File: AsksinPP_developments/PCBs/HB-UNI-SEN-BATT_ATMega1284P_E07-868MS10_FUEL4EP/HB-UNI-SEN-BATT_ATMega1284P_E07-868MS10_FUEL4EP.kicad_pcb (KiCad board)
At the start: 2 copper layers, 75 x 75 mm, 56 parts, among them J1 Conn_01x02, J10 charge, J11 ePaper connector, J12 FTDI Debuger, J2 Conn_01x02, J3 Conn_01x02, J4 Conn_01x02, J5 ISP Programmer, J6 Conn_01x04, J7 Conn_01x04, J8 Conn_01x04, J9 Conn_01x04, Q1 IRLU024N, SW1 Config button, SW2 Reset button, U1 ATmega1284P-AU, U2 TPS61221DCK, Y1 8MHz

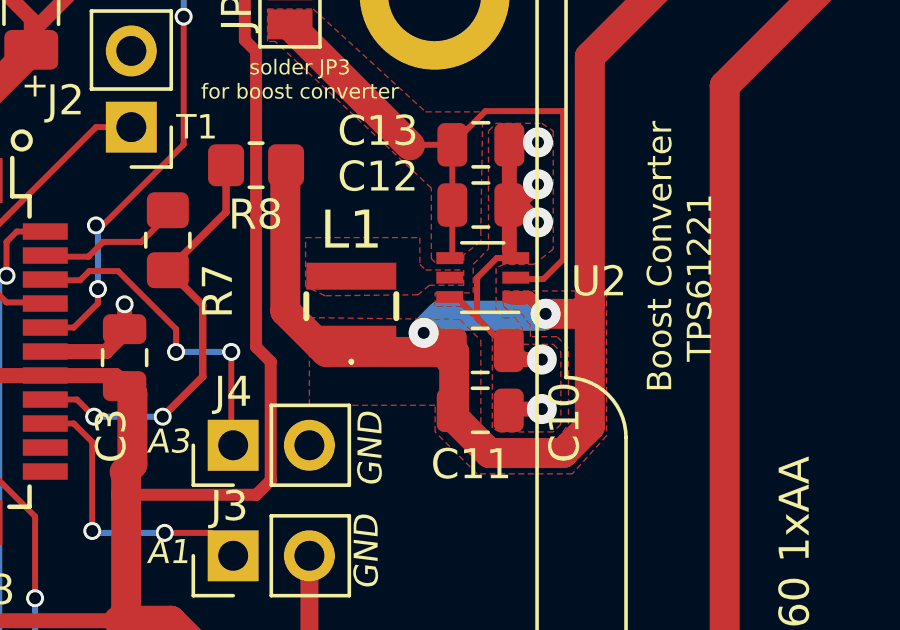
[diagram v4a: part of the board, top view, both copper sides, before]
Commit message: HB-UNI-SEN-BATT_ATMega1284P_E07-868MS10_FUEL4EP and HB-UNI-SEN-BATT_ATMega1284P_E07-868MS10_FRAM_FUEL4EP: Fix of wrong connection of EN pin of TPS61221 boost converter
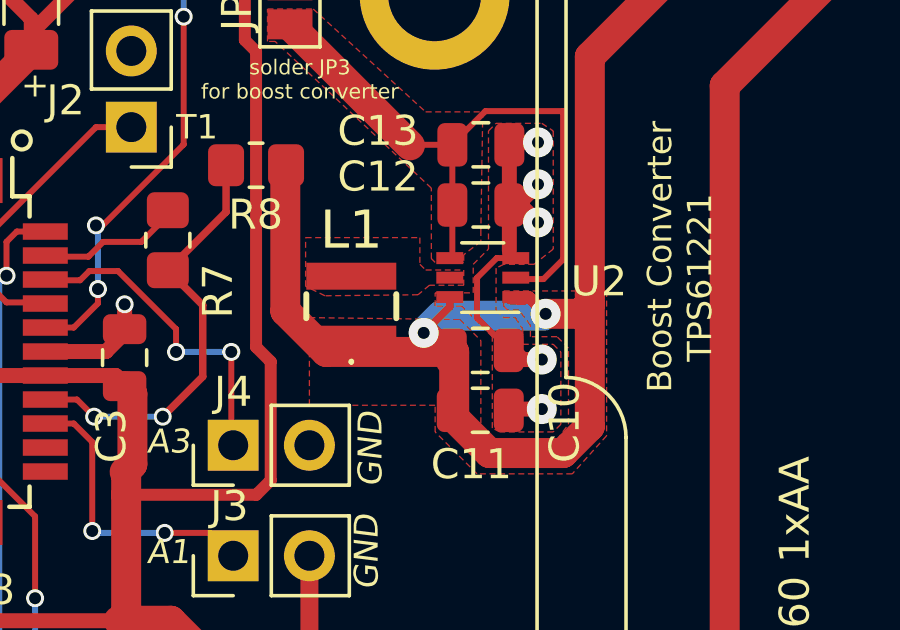
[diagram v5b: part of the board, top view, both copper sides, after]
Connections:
- U2 pad 6: GND -> /plusBAT
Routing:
- net /plusBAT: track 73.8 -> 75.3 mm
- net GND: track 140.6 -> 139.6 mm
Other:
- board text added: "Version 1.4 - 07/2023 (KiCAD 6)"
- board text removed: "Version 1.3 - 07/2023 (KiCAD 6)"
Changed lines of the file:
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@@
   (title_block
     (title "HB-UNI-SEN-BATT_ATMega1284P_E07-868MS10_FUEL4EP")
-    (date "2023-07-24")
-    (rev "1.2")
+    (date "2023-08-15")
+    (rev "1.4")
     (company "FUEL4EP")
   )
@@
     (property "Sheetname" "")
     (property "TYPE" "0")
-    (attr through_hole exclude_from_pos_files exclude_from_bom)
+    (attr through_hole exclude_from_pos_files)
     (fp_text reference "J7" (at 0 10.16) (layer "F.SilkS")
       (effects (font (size 1 1) (thickness 0.15)))
@@
     (property "Sheetname" "")
     (property "TYPE" "0")
-    (attr through_hole exclude_from_pos_files exclude_from_bom)
+    (attr through_hole exclude_from_pos_files)
     (fp_text reference "J3" (at 1.651 -0.127) (layer "F.SilkS")
       (effects (font (size 1 1) (thickness 0.15)))
@@
     (property "Sheetname" "")
     (property "TYPE" "0")
-    (attr through_hole exclude_from_pos_files exclude_from_bom)
+    (attr through_hole exclude_from_pos_files)
     (fp_text reference "J4" (at 1.778 0) (layer "F.SilkS")
       (effects (font (size 1 1) (thickness 0.15)))
@@
     (property "Sheetname" "")
     (property "TYPE" "0")
-    (attr through_hole exclude_from_pos_files exclude_from_bom)
+    (attr through_hole exclude_from_pos_files)
     (fp_text reference "J5" (at 0 -2.33 90) (layer "F.SilkS")
       (effects (font (size 1 1) (thickness 0.15)))
@@
     (property "Sheetname" "")
     (property "TYPE" "0")
-    (attr through_hole exclude_from_pos_files exclude_from_bom)
+    (attr through_hole exclude_from_pos_files)
     (fp_text reference "J8" (at 0.127 10.287) (layer "F.SilkS")
       (effects (font (size 1 1) (thickness 0.15)))
@@
       (net 44 "Net-(L1-Pad2)") (pinfunction "L") (pintype "power_in"))
     (pad "6" smd rect (at 1.1 -0.65 180) (size 0.9 0.4) (layers "F.Cu" "F.Paste" "F.Mask")
-      (net 1 "GND") (pinfunction "EN") (pintype "input"))
+      (net 18 "/plusBAT") (pinfunction "EN") (pintype "input"))
     (model "${KICAD6_3DMODEL_DIR}/Package_TO_SOT_SMD.3dshapes/SOT-363_SC-70-6.wrl"
       (offset (xyz 0 0 0))
@@
     (property "Sheetname" "")
     (property "TYPE" "0")
-    (attr through_hole exclude_from_pos_files exclude_from_bom)
+    (attr through_hole exclude_from_pos_files)
     (fp_text reference "J1" (at 2.1285 1.143) (layer "F.SilkS")
       (effects (font (size 1 1) (thickness 0.15)))
@@
     (property "Sheetname" "")
     (property "TYPE" "0")
-    (attr through_hole exclude_from_pos_files exclude_from_bom)
+    (attr through_hole exclude_from_pos_files)
     (fp_text reference "J6" (at 0.254 10.16) (layer "F.SilkS")
       (effects (font (size 1 1) (thickness 0.15)))
@@
     (property "Sheetname" "")
     (property "TYPE" "0")
-    (attr through_hole exclude_from_pos_files exclude_from_bom)
+    (attr through_hole exclude_from_pos_files)
     (fp_text reference "J2" (at 2.192 0.889) (layer "F.SilkS")
       (effects (font (size 1 1) (thickness 0.15)))
@@
     (property "Sheetname" "")
     (property "TYPE" "0")
-    (attr through_hole exclude_from_pos_files exclude_from_bom)
+    (attr through_hole exclude_from_pos_files)
     (fp_text reference "J9" (at 0 10.03) (layer "F.SilkS")
       (effects (font (size 1 1) (thickness 0.15)))
@@
   (gr_line (start 75 68) (end 75 7) (layer "Edge.Cuts") (width 0.15))
   (gr_line (start 23 0) (end 23.25 0) (layer "Edge.Cuts") (width 0.15))
-  (gr_text "Version 1.3 - 07/2023 (KiCAD 6)\n" (at 7.3945 10.773 90) (layer "B.SilkS")
+  (gr_text "Version 1.4 - 07/2023 (KiCAD 6)\n" (at 7.3945 10.773 90) (layer "B.SilkS")
     (effects (font (size 1.2 1.2) (thickness 0.2)) (justify left mirror))
   )
@@
   (segment (start 31.6515 10.519) (end 31.6515 12.1065) (width 0.5) (layer "F.Cu") (net 1))
   (segment (start 31.588 10.519) (end 32.7945 10.519) (width 0.5) (layer "F.Cu") (net 1))
-  (segment (start 52.23796 22.27896) (end 52.924 22.965) (width 0.2) (layer "F.Cu") (net 1))
   (segment (start 38.5326 24.0953) (end 40.5542 24.0953) (width 0.5) (layer "F.Cu") (net 1))
   (segment (start 55.083 26.013) (end 54.067 26.013) (width 0.5) (layer "F.Cu") (net 1))
@@
   (segment (start 52.162 24.108) (end 47.8948 24.108) (width 1) (layer "F.Cu") (net 18))
   (segment (start 54.23228 22.27896) (end 54.65096 22.27896) (width 0.4) (layer "F.Cu") (net 18))
+  (segment (start 52.0145 22.2815) (end 52.0145 22.6045) (width 0.25) (layer "F.Cu") (net 18))
   (segment (start 56.6832 22.51796) (end 56.6832 26.587402) (width 1) (layer "F.Cu") (net 18))
   (segment (start 53.33717 27.47865) (end 52.162 26.30348) (width 1) (layer "F.Cu") (net 18))
@@
   (segment (start 56.5562 22.33) (end 56.6832 22.203) (width 0.4) (layer "F.Cu") (net 18))
   (segment (start 55.21 22.838) (end 56.36316 22.838) (width 1) (layer "F.Cu") (net 18))
+  (segment (start 52.0145 22.6045) (end 51.146 23.473) (width 0.25) (layer "F.Cu") (net 18))
   (segment (start 54.489 22.33) (end 54.2956 22.33) (width 0.4) (layer "F.Cu") (net 18))
   (segment (start 46.6375 8.2815) (end 62.7261 8.2815) (width 0.4) (layer "F.Cu") (net 18))

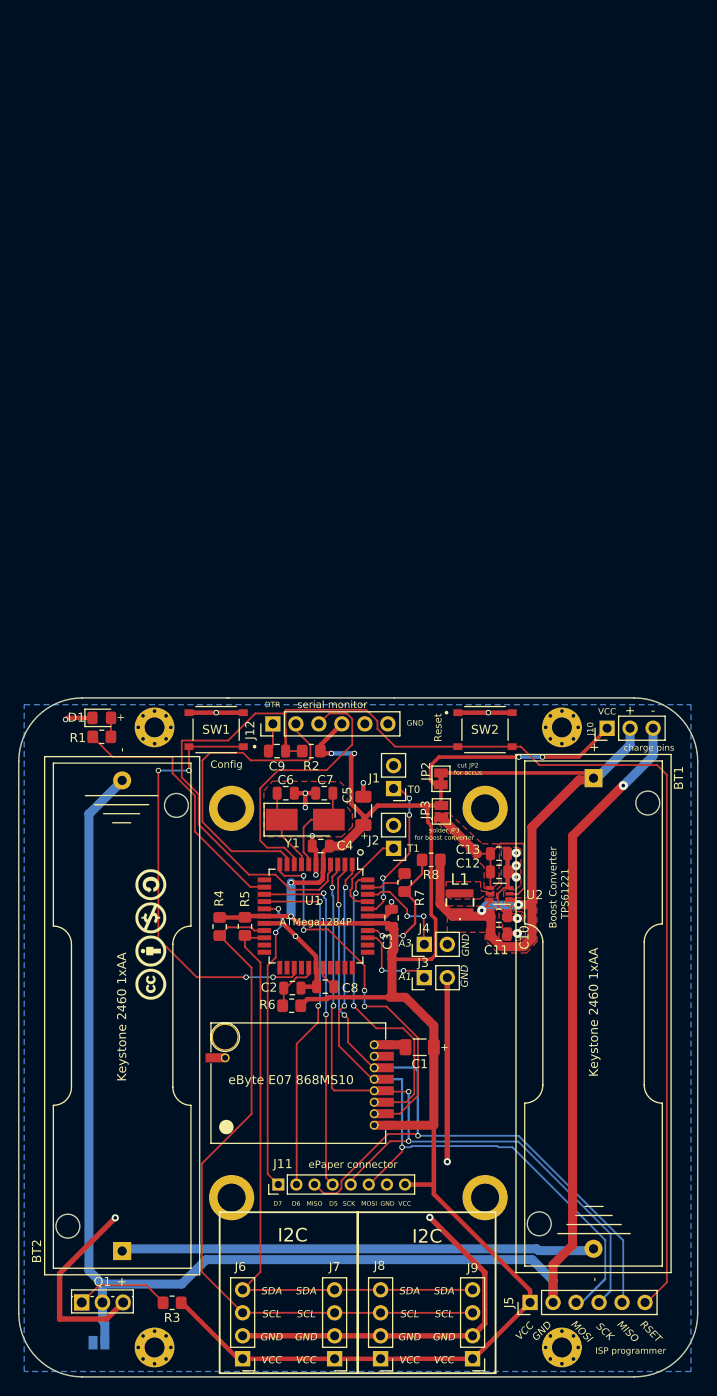
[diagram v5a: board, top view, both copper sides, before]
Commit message: PCBs: moved origin to lower left corner in order to fit to JLCPCB's scheme
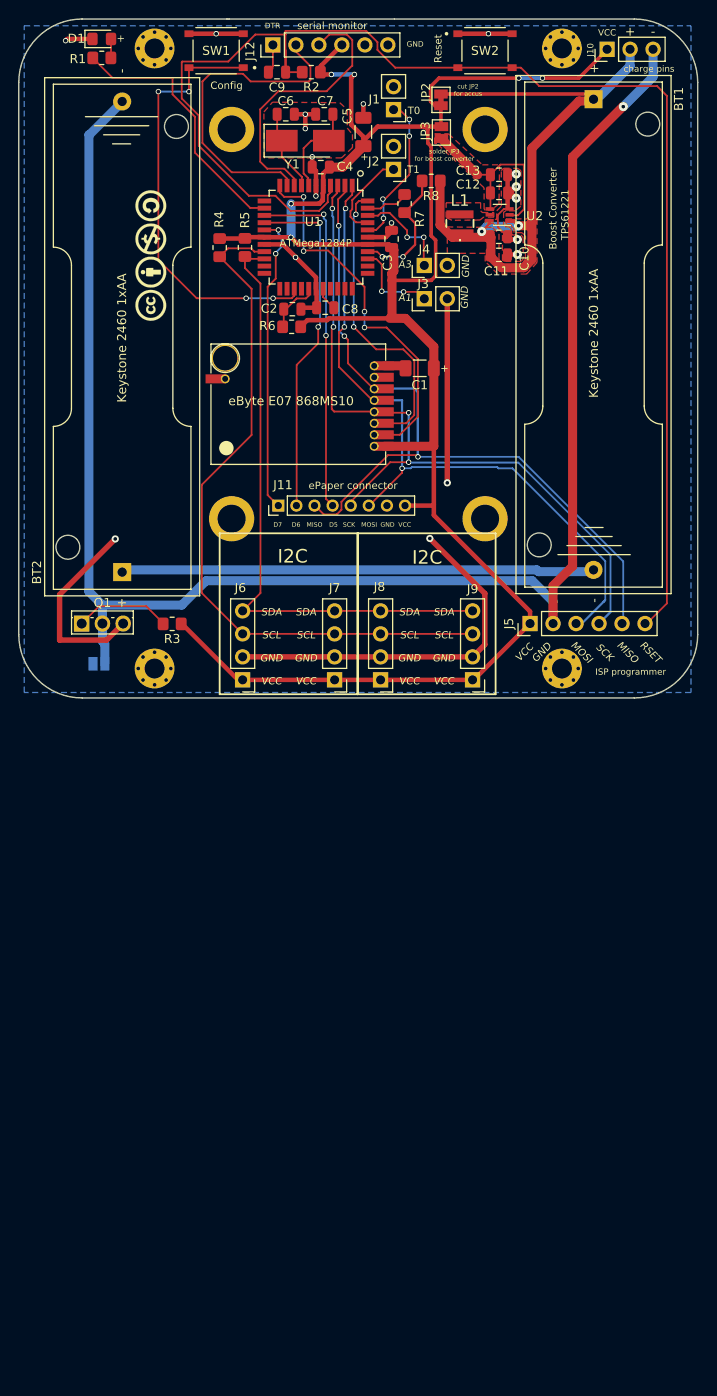
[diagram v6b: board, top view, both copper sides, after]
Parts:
- moved BT1 75.0 mm to (63.5, -66.1)
- moved BT2 75.0 mm to (11.4, -13.9)
- moved C1 75.0 mm to (44.3, -36.4)
- moved C10 75.0 mm to (53.0, -50.9)
- moved C11 75.0 mm to (53.0, -48.9)
- moved C12 75.0 mm to (53.1, -55.8)
- moved C13 75.0 mm to (53.1, -57.8)
- moved C2 75.0 mm to (30.2, -43.0)
- moved C3 75.0 mm to (41.2, -50.7)
- moved C4 75.0 mm to (33.4, -58.6)
- moved C5 75.0 mm to (38.1, -62.5)
- moved C6 75.0 mm to (29.5, -64.5)
- moved C7 75.0 mm to (33.7, -64.5)
- moved C8 75.0 mm to (33.9, -43.1)
- moved C9 75.0 mm to (28.5, -69.1)
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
